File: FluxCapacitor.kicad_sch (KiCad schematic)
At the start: 37 parts, among them J1 Jack-DC, J2 TM_1, J3 TM_2, J7 TM_1, J8 TM_1, U1 OKI-78SR-5_1.5-W36-C, U2 ESP32_DEVBOARD

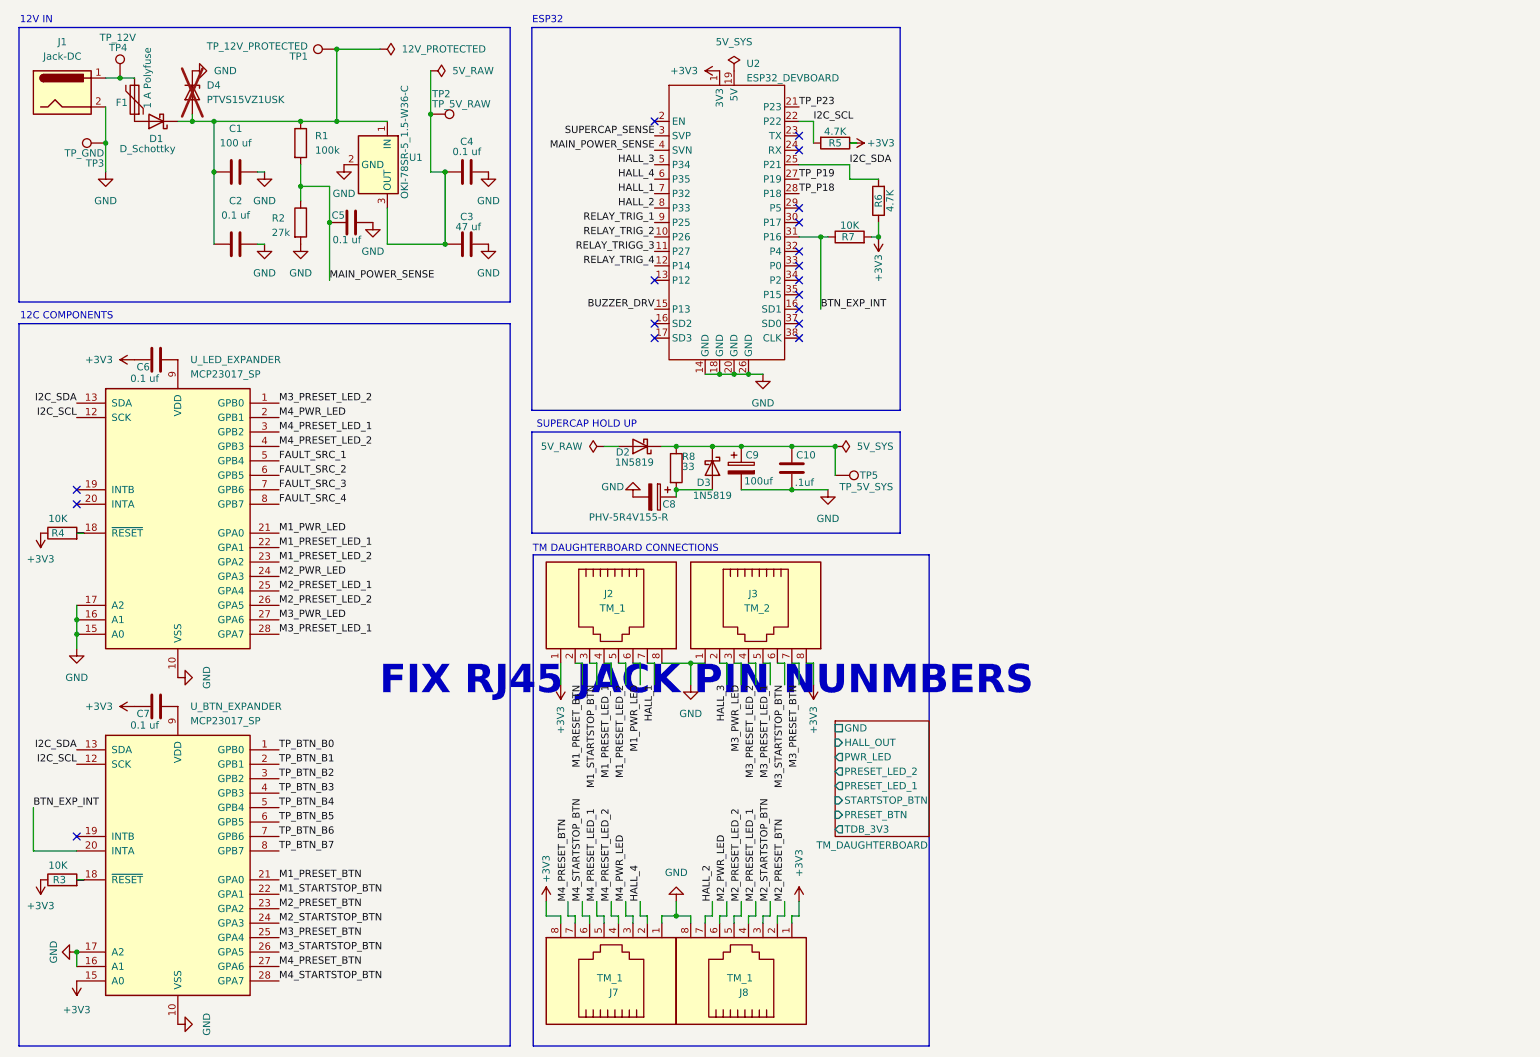
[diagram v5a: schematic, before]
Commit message: Fixed various issues
-Fixed RJ45 daughterboard connector pinouts on mainboard
-fixed caps on vcc of the I2C GPIO expanders
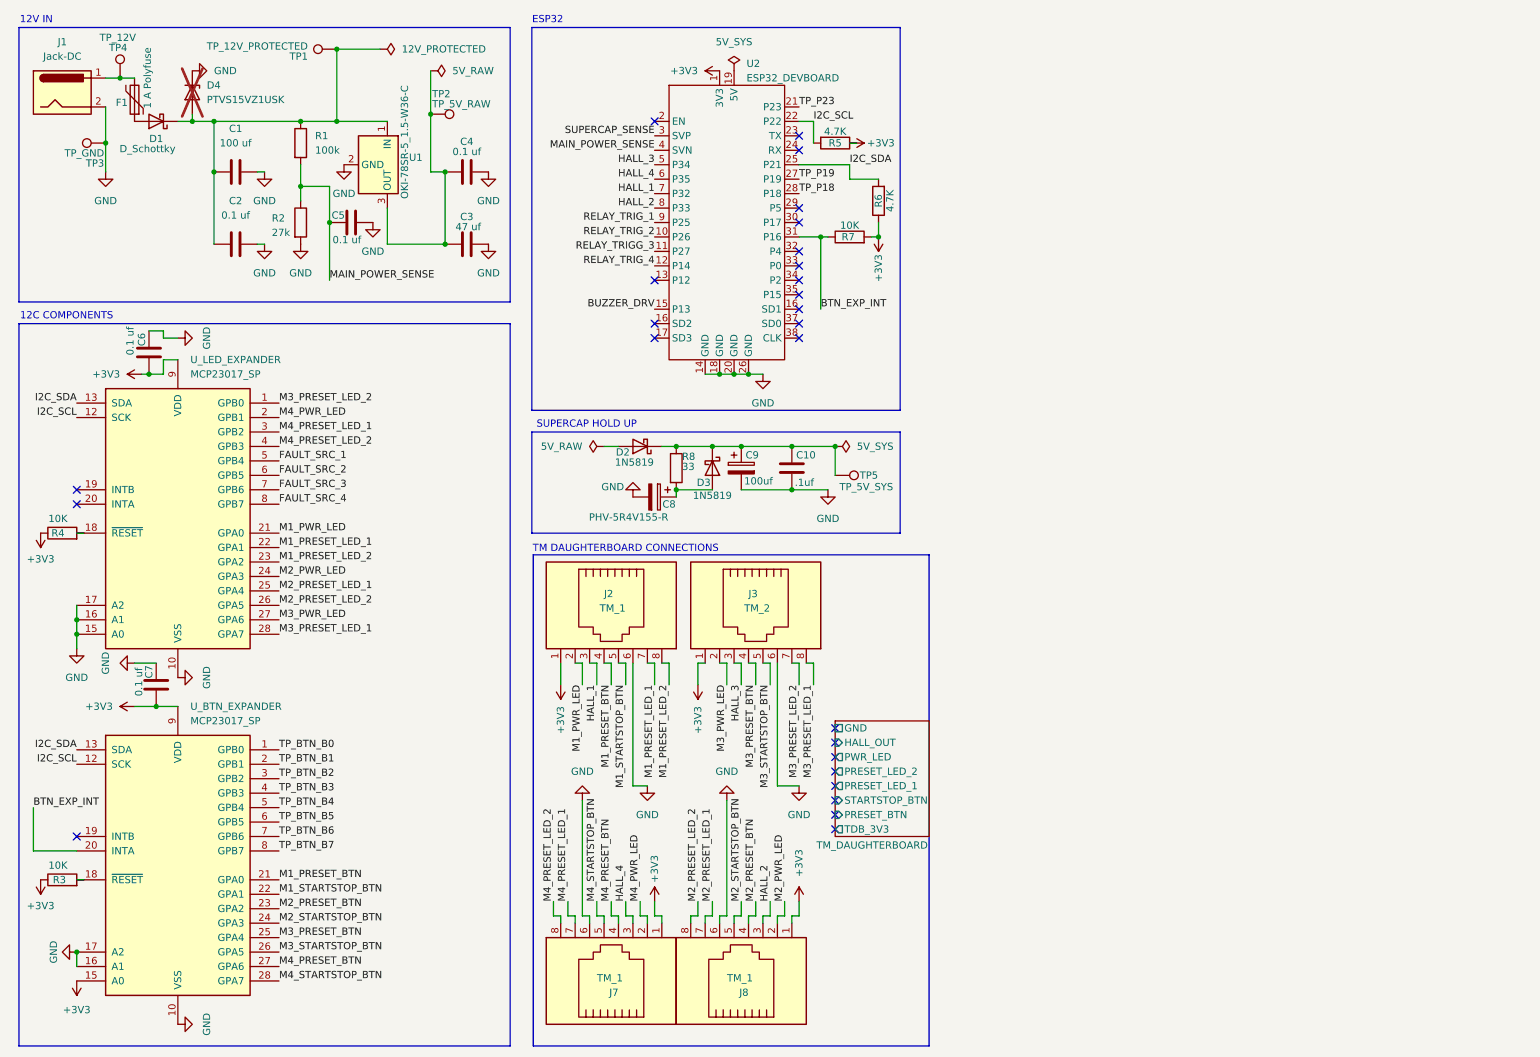
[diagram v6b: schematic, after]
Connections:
- net +3V3: now also C6.2, C7.2, J3.1, J7.1, U_BTN_EXPANDER.9 (VDD), U_LED_EXPANDER.9 (VDD); no longer C6.1, C7.1, J3.8, J7.8
- net GND: now also C6.1, C7.1, J2.6, J3.6, J7.6, J8.6; no longer J2.8, J3.1, J7.1, J8.8
- net HALL_1: now also J2.3; no longer J2.7
- net HALL_2: now also J8.3; no longer J8.7
- net HALL_3: now also J3.3; no longer J3.2
- net HALL_4: now also J7.3; no longer J7.2
- net M1_PRESET_BTN: now also J2.4; no longer J2.2
- net M1_PRESET_LED_1: now also J2.7; no longer J2.4
- net M1_PRESET_LED_2: now also J2.8; no longer J2.5
- net M1_PWR_LED: now also J2.2; no longer J2.6
- net M1_STARTSTOP_BTN: now also J2.5; no longer J2.3
- net M2_PRESET_BTN: now also J8.4; no longer J8.2
- net M2_PRESET_LED_1: now also J8.7; no longer J8.4
- net M2_PRESET_LED_2: now also J8.8; no longer J8.5
- net M2_PWR_LED: now also J8.2; no longer J8.6
- net M2_STARTSTOP_BTN: now also J8.5; no longer J8.3
- net M3_PRESET_BTN: now also J3.4; no longer J3.7
- net M3_PRESET_LED_1: now also J3.8; no longer J3.5
- net M3_PRESET_LED_2: now also J3.7; no longer J3.4
- net M3_PWR_LED: now also J3.2; no longer J3.3
- net M3_STARTSTOP_BTN: now also J3.5; no longer J3.6
- net M4_PRESET_BTN: now also J7.4; no longer J7.7
- net M4_PRESET_LED_1: now also J7.7; no longer J7.5
- net M4_PRESET_LED_2: now also J7.8; no longer J7.4
- net M4_PWR_LED: now also J7.2; no longer J7.3
- net M4_STARTSTOP_BTN: now also J7.5; no longer J7.6
- no-connect marks 18 -> 26
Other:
- note removed: "FIX RJ45 JACK PIN NUNMBERS"
- moved on the sheet: C6, C7

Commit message: Misc save
Started relay-related boards
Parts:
- added J9: RELAY, symbol Connector:RJ45
- added TP6, TP7: TP_TX, symbol Connector:TestPoint
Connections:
- net GND: now also J9.2, J9.5
- net RELAY_TRIGG_3: now also J9.7
- net RELAY_TRIG_1: now also J9.3
- net RELAY_TRIG_2: now also J9.6
- net RELAY_TRIG_4: now also J9.8
- net at U2.23 (TX): now also TP6.1
- net at U2.24 (RX): now also TP7.1
- no-connect marks 26 -> 24
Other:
- added sheet RELAY DAUGHTERBOARD (Relay_Daughterboard.kicad_sch)
- added sheet RELAY SIGNAL SPLITTER (RELAY_SIGNAL_SPLITTER.kicad_sch)
- note added: "RELAY DAUGHTERBOARD CONNECTION"
- note added: "RELAY SIGNAL SPLITTER"
- moved on the sheet: C10, C8, C9, D2, D3, R5, R6, R7, R8, TP5, U2

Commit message: Relay work
did all the relay related work
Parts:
- added C11: 10UF, symbol Device:C_Polarized
- added C12: .1uf, symbol Device:C
- added D5: 1N4148, Diode_THT:D_DO-35_SOD27_P7.62mm_Horizontal, symbol Diode:1N4148
- added D6: LED, symbol Device:LED
- added D7: P6KE15A, Diode_SMD:Nexperia_DSN1608-2_1.6x0.8mm, symbol Diode:PTVS15VZ1USK
- added J10: RELAY, symbol Connector:RJ45
- added J19, J20, J21, J22, J23: Conn_01x03_Socket, symbol Connector:Conn_01x03_Socket
- added J4: Conn_01x02, symbol Connector_Generic:Conn_01x02
- added K1: G5V-1, Relay_THT:Relay_SPDT_Omron_G5V-1, symbol Relay:G5V-1
- added Q1: 2N7000, Q_TO-92_135AN_OSI, symbol Generic:2N7000
- added R10: 100K, symbol Device:R
- added R11: 10K, symbol Device:R
- added R9: 100Ω, symbol Device:R
- added SW1: SW_SPDT_321, symbol Switch:SW_SPDT_321
- added TP10: TP_RLY_NO, symbol Connector:TestPoint
- added TP11: TP_NC, symbol Connector:TestPoint
- added TP12: TP_12V, symbol Connector:TestPoint
- added TP13: TP_GND, symbol Connector:TestPoint
- added TP14: TP_RLY_GATE, symbol Connector:TestPoint
- added TP8: TP_RLY_NC, symbol Connector:TestPoint
- added TP9: TP_RLY_COM, symbol Connector:TestPoint
- D4: value PTVS15VZ1USK -> P6KE15A; now fitted
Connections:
- net GND: now also C11.2, C12.2, D7.2 (A), J10.2, J10.5, J19.3 (Pin_3), J20.3 (Pin_3), J21.3 (Pin_3), J22.3 (Pin_3), J23.3 (Pin_3), Q1.1 (S), R10.1, SW1.1 (C), TP13.1
- new net: J4.1 (Pin_1), K1.1, TP8.1
- new net: J4.2 (Pin_2), K1.5, K1.6, TP9.1
- new net: D5.1 (K), D6.1 (K), K1.2, TP12.1
- new net: D6.2 (A), R11.1
- new net: D5.2 (A), K1.9, Q1.3 (D), R11.2, SW1.2 (B)
- new net: SW1.3 (A), TP11.1
- new net: Q1.2 (G), R10.2, R9.2, TP14.1
- new net: C11.1, C12.1, D7.1 (K), J20.2 (Pin_2)
- new net: K1.10, TP10.1
- new net DB_RELAY_TRIGG_3: J10.7
- new net DB_RELAY_TRIG_1: J10.3, J23.1 (Pin_1)
- new net DB_RELAY_TRIG_2: J10.6, J22.1 (Pin_1)
- new net DB_RELAY_TRIG_3: J21.1 (Pin_1)
- new net DB_RELAY_TRIG_4: J10.8, J19.1 (Pin_1)
- new net RLY_TRIGGER: J20.1 (Pin_1), R9.1
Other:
- removed sheet RELAY DAUGHTERBOARD
- removed sheet RELAY SIGNAL SPLITTER
- note added: "DEBUGGING AND FAULT LEDS"
- note added: "INPUT"
- note added: "MAINBORAD CONNECTION"
- note added: "RELAY BOARD"
- note added: "RELAY LOGIC"
- note added: "RELAY RELATED DAUGHTERBOARDS"
- note added: "TM CONTROL PANEL 1"
- note added: "TM CONTROL PANEL 2"
- note added: "TM CONTROL PANEL 3"
- note added: "TM CONTROL PANEL 4"
- company: (none) -> HEELUXE
- title: (none) -> FLUX CAPACITOR
